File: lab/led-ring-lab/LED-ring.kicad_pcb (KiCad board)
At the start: 2 copper layers, 80 x 80 mm, 16 parts, among them U1 atmega328p

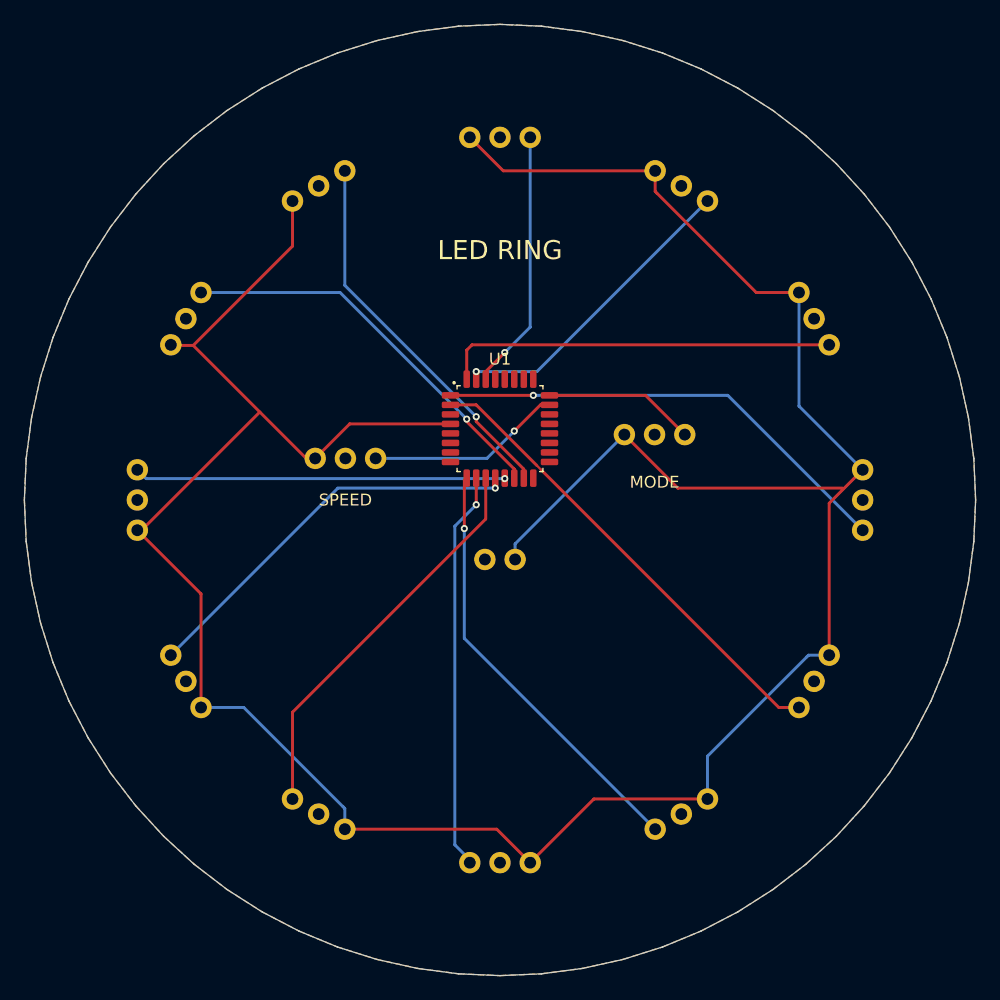
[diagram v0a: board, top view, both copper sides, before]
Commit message: lab: every board is a real board: an Arduino Nano and registry parts, routed, ready to order
The lab boards ran on simulation-only envelopes (labMcu, labDisplay, a battery). Now each is
an Arduino Nano on two sockets on the back (flashed over its USB, the image the app builds),
its lights LEDs through 1 kΩ, its knobs PTV09A pots, its display the MAX7219 eight-digit
module, its sensors an SHT31 and an SCD40 with their datasheets' support circuits, the FTDI
header for the serial console; the servo boards take 5 V on a screw terminal with a bulk
capacitor. All ten check complete with no errors or warnings, their firmware unchanged
(serial-device now on the 328P), and run in the lab without a fault (3 s each, dev host).

The registry: every interactive board must be ready to order and flash (publish.mjs refuses
one that is not; status simulation-only removed).

Claude-Session: https://claude.ai/code/session_01ATmMmxyrWxFwR3nTdXUrcx
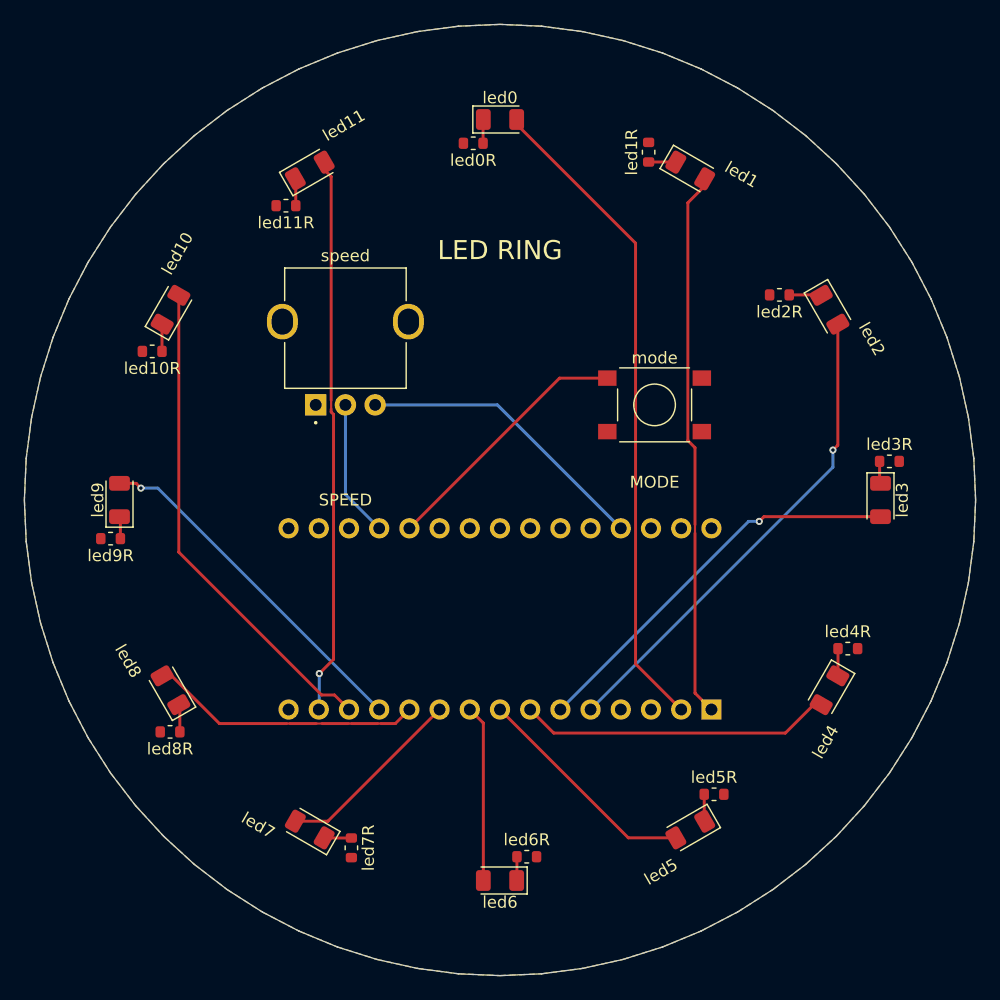
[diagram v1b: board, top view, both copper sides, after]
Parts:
- removed battery: battery, Regulated battery module
- removed the mode at (153.0, 152.0)
- removed the speed at (127.0, 152.0)
- added led0R: 1kohm, R_0603_1608Metric, F.Cu at (137.8, 130.0)
- added led10R: 1kohm, R_0603_1608Metric, F.Cu at (110.8, 147.5)
- added led11R: 1kohm, R_0603_1608Metric, F.Cu at (122.0, 135.2)
- added led1R: 1kohm, R_0603_1608Metric, F.Cu at (152.5, 130.8)
- added led2R: 1kohm, R_0603_1608Metric, F.Cu at (163.5, 142.8)
- added led3R: 1kohm, R_0603_1608Metric, F.Cu at (172.8, 156.8)
- added led4R: 1kohm, R_0603_1608Metric, F.Cu at (169.2, 172.5)
- added led5R: 1kohm, R_0603_1608Metric, F.Cu at (158.0, 184.8)
- added led6R: 1kohm, R_0603_1608Metric, F.Cu at (142.2, 190.0)
- added led7R: 1kohm, R_0603_1608Metric, F.Cu at (127.5, 189.2)
- added led8R: 1kohm, R_0603_1608Metric, F.Cu at (112.2, 179.5)
- added led9R: 1kohm, R_0603_1608Metric, F.Cu at (107.2, 163.2)
- added mode: PTS645SM43SMTR92 LFS, SW_Tactile_SPST_6x6mm_SMD, F.Cu at (153.0, 152.0)
- added speed: PTV09A-4020F-B103, Potentiometer_Bourns_PTV09A-4_Vertical, F.Cu at (127.0, 152.0)
- U1: value atmega328p -> A000005; footprint TQFP-32_7x7mm_P0.8mm -> Arduino_Nano_Socket_2x15_P2.54mm_W15.24mm; moved to B.Cu
- led0, led1, led2, led3: value indicator -> green; footprint Indicator module -> LED_1206_3216Metric
- led10, led11, led8, led9: value indicator -> red; footprint Indicator module -> LED_1206_3216Metric
- led4, led5, led6, led7: value indicator -> orange; footprint Indicator module -> LED_1206_3216Metric
- moved U1 16.0 mm to (140.0, 170.0), turned to 90 degrees
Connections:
- U1 pad 1: L3 -> L1
- U1 pad 10: L6 -> L7
- U1 pad 11: L7 -> L8
- U1 pad 12: L8 -> L9
- U1 pad 13: L9 -> L10
- U1 pad 14: L10 -> L11
- U1 pad 15: L11 -> (no net)
- U1 pad 19: (no net) -> SPEED
- U1 pad 2: L4 -> L0
- U1 pad 20: (no net) -> MODE
- U1 pad 23: SPEED -> (no net)
- U1 pad 24: MODE -> (no net)
- U1 pad 27: (no net) -> V5
- U1 pad 29: (no net) -> GND
- U1 pad 3: GND -> (no net)
- U1 pad 30: L0 -> (no net)
- U1 pad 4: V5 -> GND
- U1 pad 5: (no net) -> L2
- U1 pad 6: (no net) -> L3
- U1 pad 7: (no net) -> L4
- U1 pad 8: (no net) -> L5
- U1 pad 9: L5 -> L6
- led0 pad 1: V5 -> L0_K
- led0 pad 2: GND -> L0
- led1 pad 1: V5 -> L1_K
- led1 pad 2: GND -> L1
- led10 pad 1: V5 -> L10_K
- led10 pad 2: GND -> L10
- led11 pad 1: V5 -> L11_K
- led11 pad 2: GND -> L11
- led2 pad 1: V5 -> L2_K
- led2 pad 2: GND -> L2
- led3 pad 1: V5 -> L3_K
- led3 pad 2: GND -> L3
- led4 pad 1: V5 -> L4_K
- led4 pad 2: GND -> L4
- led5 pad 1: V5 -> L5_K
- led5 pad 2: GND -> L5
- led6 pad 1: V5 -> L6_K
- led6 pad 2: GND -> L6
- led7 pad 1: V5 -> L7_K
- led7 pad 2: GND -> L7
- led8 pad 1: V5 -> L8_K
- led8 pad 2: GND -> L8
- led9 pad 1: V5 -> L9_K
- led9 pad 2: GND -> L9
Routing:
- net V5: track 245.1 -> 25.0 mm
- net L0: track 21.9 -> 55.4 mm, vias 1 -> 0
- net L1: track 25.4 -> 46.0 mm, vias 1 -> 0
- net L6: track 33.6 -> 14.9 mm, vias 1 -> 0
- net L7: track 33.7 -> 16.0 mm
- net L5: track 36.3 -> 19.3 mm, vias 1 -> 0
- net L11: track 32.1 -> 46.9 mm
- net L4: track 39.8 -> 26.3 mm
- net L8: track 34.8 -> 22.9 mm, vias 1 -> 0
- net MODE: track 12.7 -> 21.9 mm
- net L10: track 33.4 -> 41.4 mm, vias 1 -> 0
- net L2: track 33.1 -> 41.0 mm, vias 0 -> 1
- net L3: track 39.4 -> 33.6 mm
- net SPEED: track 16.5 -> 11.6 mm, vias 1 -> 0
- net L2_K: track 0.00 -> 2.70 mm
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
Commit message: registry: every board rebuilt with pcbkit main 4684674e6 - the bought part named on the board
pcbkit dc07fdfd6 writes the bought row's MPN and Manufacturer (the design's own kept as DesignMPN /
DesignManufacturer) and the build chooses parts before it places (6361ec104). Each of the 44 boards
was rebuilt (; the two P4 boards  only: their builds reroute pairs):
copper unchanged on all 44 (segments, arcs and vias counted before and after), placement kept; the
Arduino and lab boards now carry the parts the catalogue gives them. The check gains only the new
judgements: part-maker (a part bought from another maker) and part-missing on hand-fitted modules
(DS1 sockets); p4-touch-7 loses part-stale. The P4 boards keep their hole-clearance errors (a
reroute is Team 3's).

Claude-Session: https://claude.ai/code/session_01BAgp959tApA8aEg85EYgfb
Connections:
- mode pad 2: MODE -> GND
